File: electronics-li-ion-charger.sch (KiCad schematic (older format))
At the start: 17 parts, among them J1 Conn_01x01_Male, J2 Conn_01x01_Male, J3 USB_B_Micro, J4 Conn_01x03_Male, U1 MCP73831-2-OT

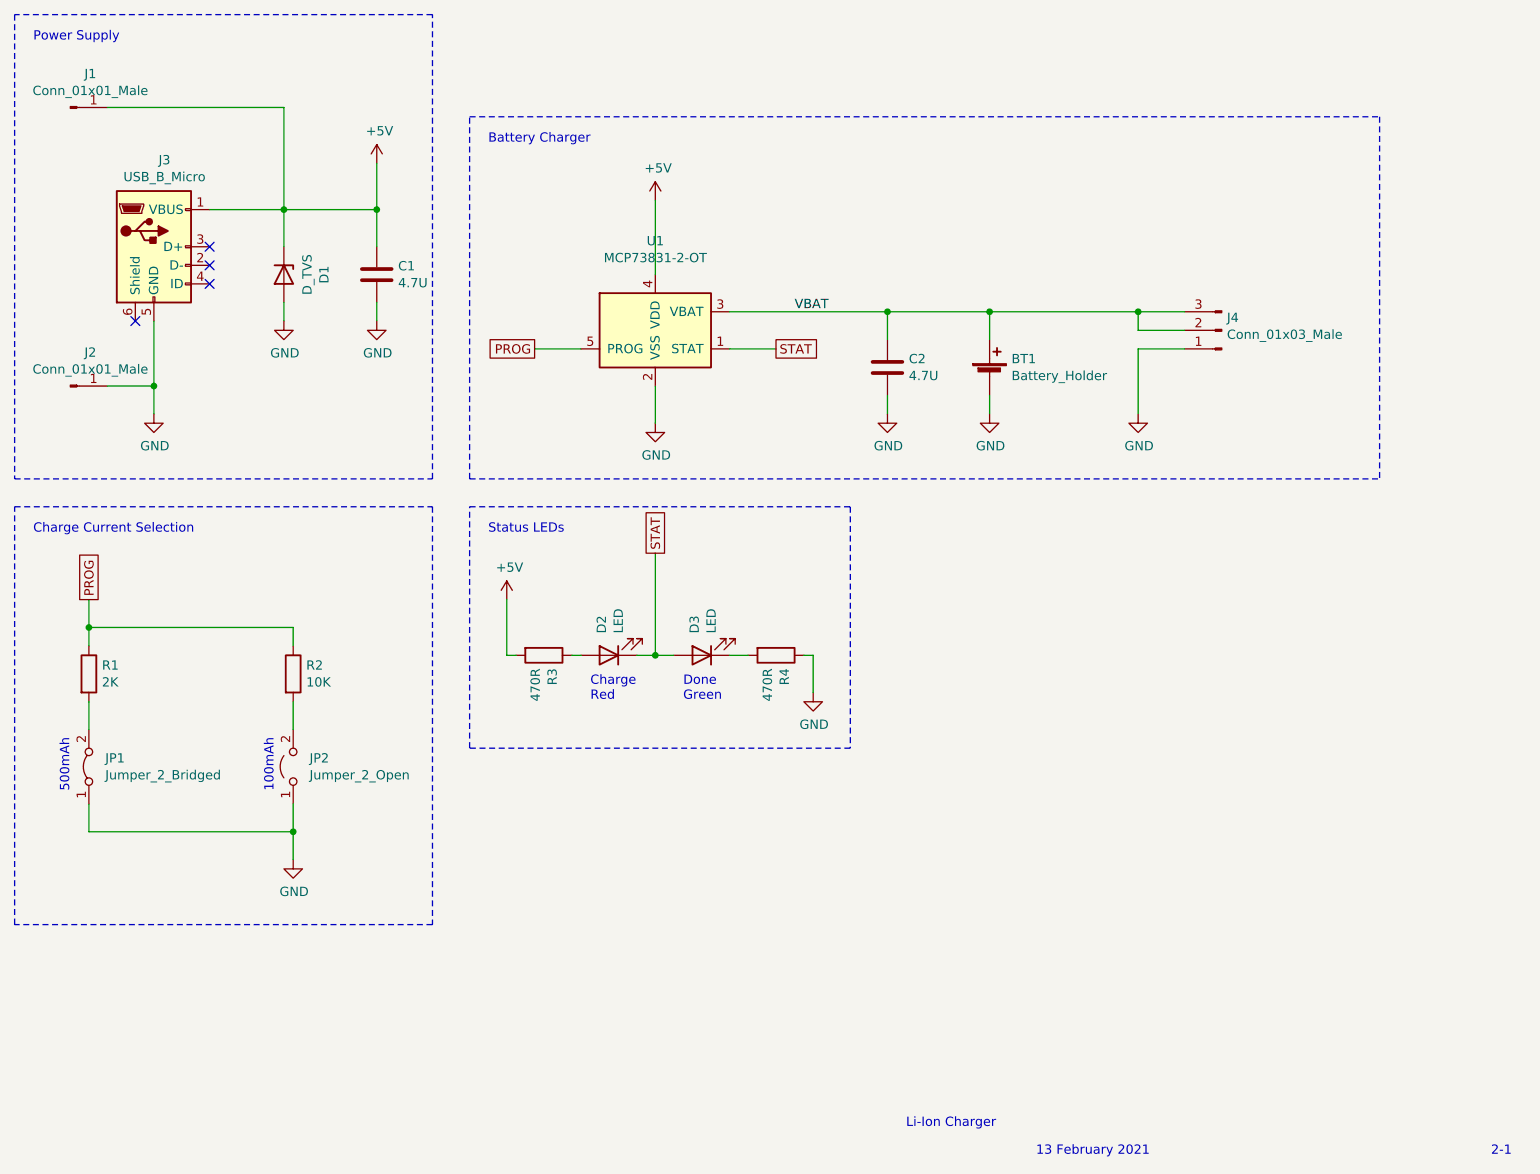
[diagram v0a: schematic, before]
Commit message: Rev3-0: Add reverse polarity protection.
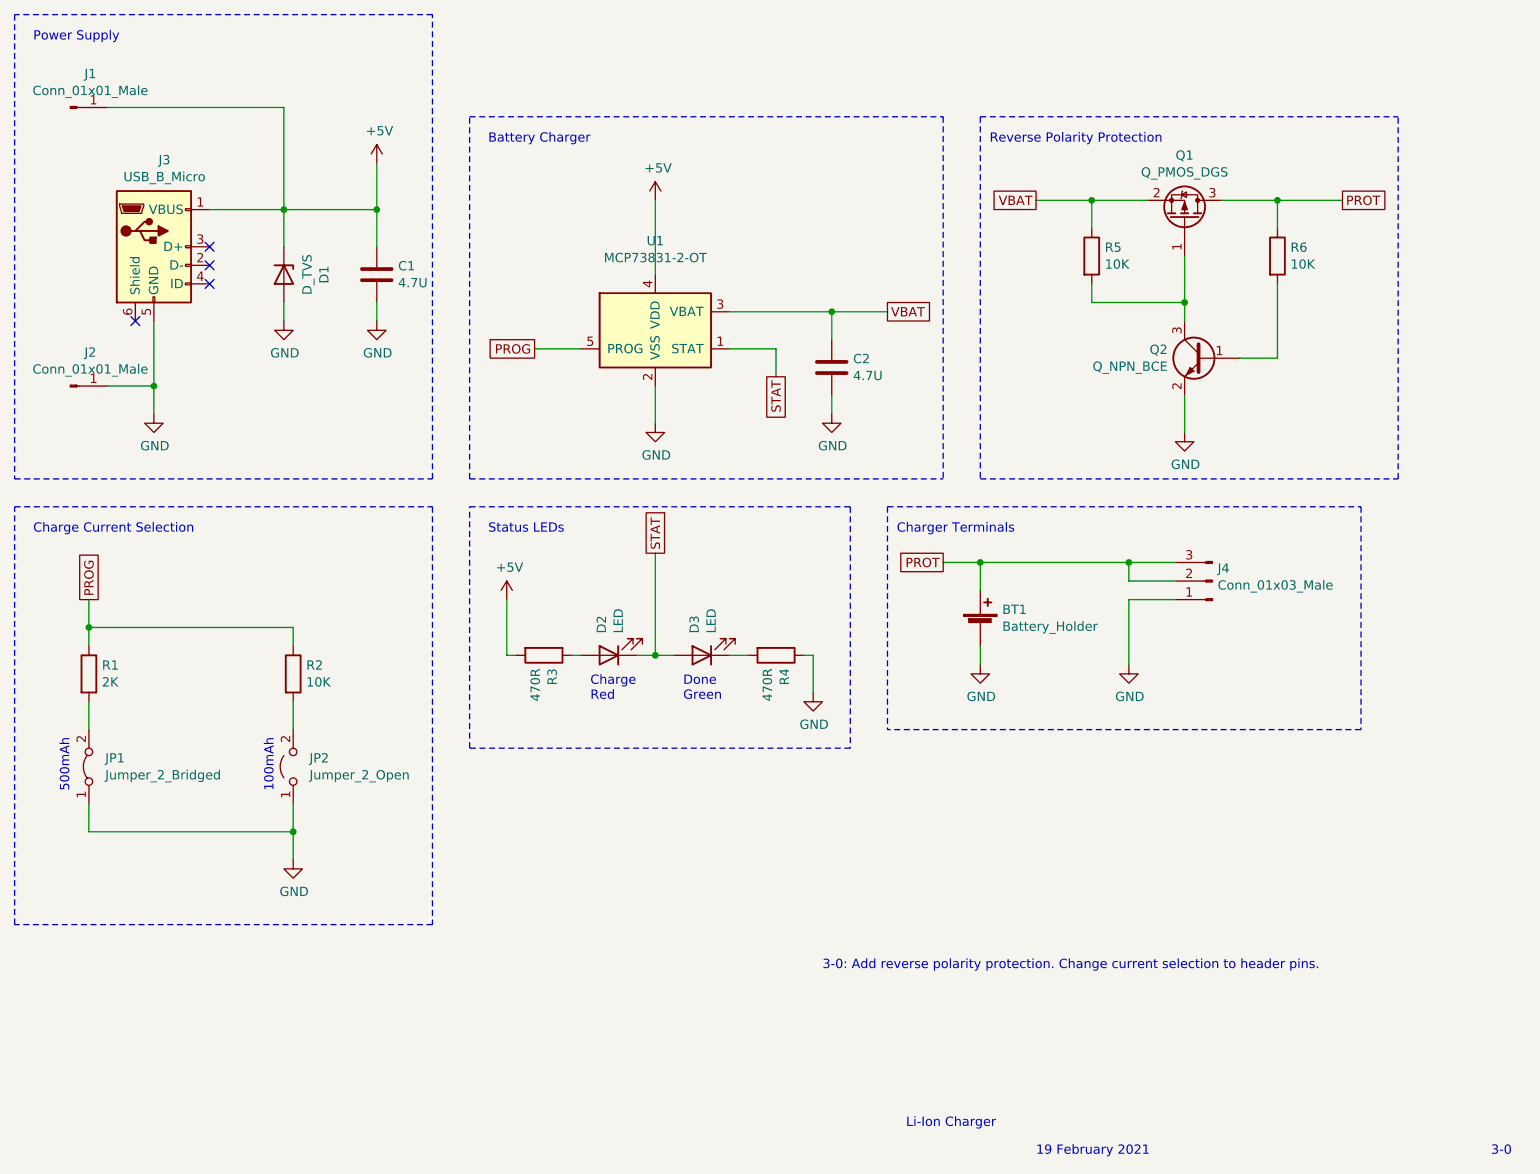
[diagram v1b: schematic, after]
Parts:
- added Q1: Q_PMOS_DGS, Package_TO_SOT_SMD:SOT-23_Handsoldering, symbol Device:Q_PMOS_GSD
- added Q2: Q_NPN_BCE, Package_TO_SOT_SMD:SOT-23_Handsoldering, symbol Device:Q_NPN_BEC
- added R5, R6: 10K, Resistor_SMD:R_1206_3216Metric_Pad1.30x1.75mm_HandSolder, symbol Device:R
- JP1, JP2: footprint Jumper:SolderJumper-2_P1.3mm_Open_TrianglePad1.0x1.5mm -> Connector_PinHeader_2.54mm:PinHeader_1x02_P2.54mm_Vertical
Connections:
- net GND: now also Q2.2 (E)
- net VBAT: now also Q1.2 (S), R5.1; no longer BT1.1 (+), J4.2 (Pin_2), J4.3 (Pin_3)
- new net: Q2.1 (B), R6.2
- new net: Q1.1 (G), Q2.3 (C), R5.2
- new net PROT: BT1.1 (+), J4.2 (Pin_2), J4.3 (Pin_3), Q1.3 (D), R6.1
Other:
- note added: "19 February 2021"
- note added: "3-0"
- note added: "3-0: Add reverse polarity protection. Change current selection to header pins."
- note added: "Charger Terminals"
- note added: "Reverse Polarity Protection"
- note removed: "13 February 2021"
- note removed: "2-1"
- moved on the sheet: BT1, C2, J4
